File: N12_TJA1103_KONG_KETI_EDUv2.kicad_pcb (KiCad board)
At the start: 2 copper layers, 33 x 57 mm, 65 parts, among them IC1 TJA1103AHN, J1 Conn_02x02_Odd_Even, J2 Conn_02x11_Odd_Even, J3 9-2304372-9, J4 E6S20A-40MT5-Z, Q1 FDN340P, Q2 BSS138, SW2 SW-DIP-ANGLED DS03-254-02BE, Y1 Crystal_GND24_Small

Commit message: fix: finalize native routing and TJA1103 power pin mapping
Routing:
- net Earth: track 24.8 -> 51.6 mm, vias 0 -> 1
- net /TX_EN: track 5.42 -> 26.6 mm, vias 0 -> 2
- net /DP+: track 11.5 -> 20.4 mm, vias 0 -> 1
- net /GP0/CONF0/nLINKLED: track 53.9 -> 56.4 mm
- net /DN-: track 13.7 -> 15.8 mm

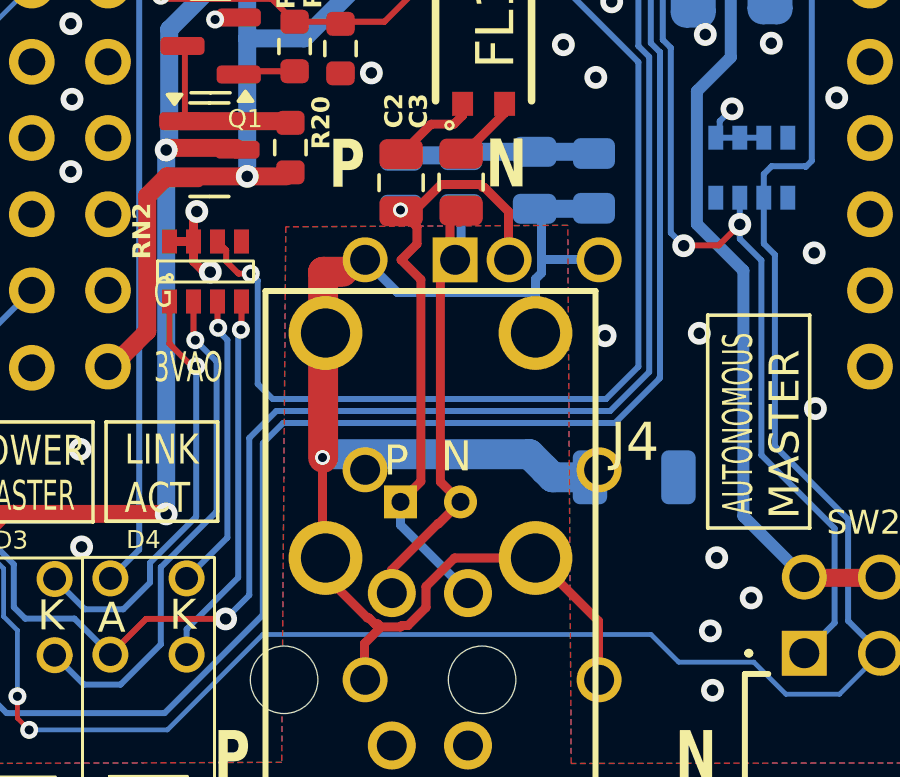
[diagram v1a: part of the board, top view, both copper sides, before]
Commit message: fix: correct MATEnet differential pair polarity
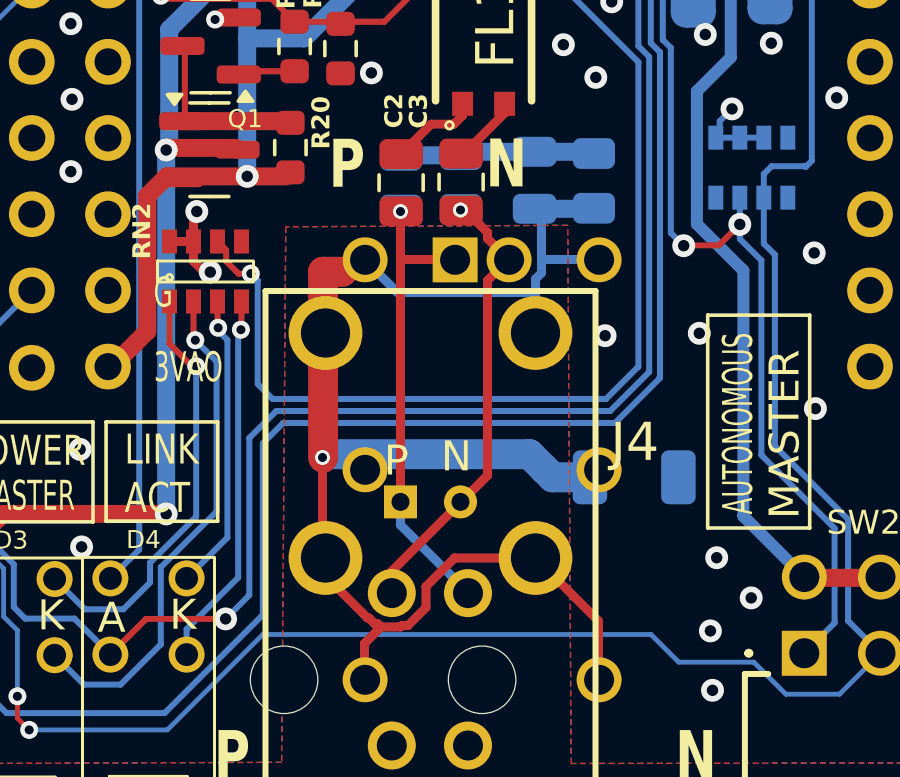
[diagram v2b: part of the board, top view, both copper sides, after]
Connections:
- J3 pad 1: /DN- -> /DP+
- J3 pad 2: /DP+ -> /DN-
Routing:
- net /DP+: track 20.4 -> 15.4 mm
- net /DN-: track 15.8 -> 15.1 mm, vias 0 -> 1
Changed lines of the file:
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@@
 			(layers "*.Cu" "*.Mask")
 			(remove_unused_layers no)
-			(net "/DN-")
+			(net "/DP+")
 			(pinfunction "DN-")
 			(pintype "passive")
@@
 			(layers "*.Cu" "*.Mask")
 			(remove_unused_layers no)
-			(net "/DP+")
+			(net "/DN-")
 			(pinfunction "DP+")
 			(pintype "passive")
@@
 	)
 	(segment
-		(start 16.65 38.79)
-		(end 17.02 39.16)
-		(width 0.3)
-		(layer "F.Cu")
-		(net "/DN-")
-	)
-	(segment
-		(start 16.25 48.15)
-		(end 14.7 49.7)
+		(start 17.15 37.7)
+		(end 17 37.7)
 		(width 0.3)
 		(layer "F.Cu")
@@
 	)
 	(segment
-		(start 16.82 39.36)
-		(end 16.33 39.85)
+		(start 17.9 40.05)
+		(end 17.9 46.55)
 		(width 0.3)
 		(layer "F.Cu")
@@
 	)
 	(segment
-		(start 16.27 48.16)
-		(end 16.25 48.15)
+		(start 17.9 38.65)
+		(end 17.9 38.45)
 		(width 0.3)
 		(layer "F.Cu")
@@
 	)
 	(segment
-		(start 16.65 38.09)
-		(end 16.65 38.79)
+		(start 17 47.45)
+		(end 14.7 49.75)
 		(width 0.3)
 		(layer "F.Cu")
@@
 	)
 	(segment
-		(start 16.33 46.76)
-		(end 17 47.43)
+		(start 17.9 46.55)
+		(end 17 47.45)
 		(width 0.3)
 		(layer "F.Cu")
@@
 	)
 	(segment
-		(start 14.7 49.7)
-		(end 14.7 50.45)
+		(start 17.9 38.45)
+		(end 17.15 37.7)
 		(width 0.3)
 		(layer "F.Cu")
@@
 	)
 	(segment
-		(start 17.02 37.72)
-		(end 16.65 38.09)
+		(start 18.6 39.35)
+		(end 17.9 40.05)
 		(width 0.3)
 		(layer "F.Cu")
@@
 	)
 	(segment
-		(start 16.33 39.85)
-		(end 16.33 46.76)
+		(start 14.7 49.75)
+		(end 14.7 50.45)
 		(width 0.3)
 		(layer "F.Cu")
@@
 	)
 	(segment
-		(start 17 47.43)
-		(end 16.27 48.16)
+		(start 18.6 39.35)
+		(end 17.9 38.65)
 		(width 0.3)
 		(layer "F.Cu")
 		(net "/DN-")
 	)
-	(segment
-		(start 17.02 37.6825)
-		(end 17.02 39.16)
-		(width 0.3)
-		(layer "B.Cu")
+	(via
+		(at 17 37.7)
+		(size 0.5)
+		(drill 0.3)
+		(layers "F.Cu" "B.Cu")
+		(tenting
+			(front yes)
+			(back yes)
+		)
 		(net "/DN-")
 	)
@@
 	)
 	(segment
-		(start 15.25 37.95)
-		(end 16.35 36.85)
-		(width 0.3)
-		(layer "F.Cu")
-		(net "/DP+")
-	)
-	(segment
-		(start 15.02 37.74)
-		(end 15.55 38.27)
-		(width 0.3)
-		(layer "F.Cu")
-		(net "/DP+")
-	)
-	(segment
-		(start 15.55 38.27)
-		(end 15.55 38.83)
-		(width 0.3)
-		(layer "F.Cu")
-		(net "/DP+")
-	)
-	(segment
-		(start 17.8 36.95)
-		(end 18.6 37.75)
-		(width 0.3)
-		(layer "F.Cu")
-		(net "/DP+")
-	)
-	(segment
-		(start 15.68 46.75)
-		(end 15.68 40.02)
-		(width 0.3)
-		(layer "F.Cu")
-		(net "/DP+")
-	)
-	(segment
-		(start 15.55 38.83)
-		(end 15.02 39.36)
-		(width 0.3)
-		(layer "F.Cu")
-		(net "/DP+")
-	)
-	(segment
-		(start 18.6 37.75)
-		(end 18.6 39.35)
-		(width 0.3)
-		(layer "F.Cu")
-		(net "/DP+")
-	)
-	(segment
-		(start 17.75 36.95)
-		(end 17.8 36.95)
-		(width 0.3)
-		(layer "F.Cu")
-		(net "/DP+")
-	)
-	(segment
-		(start 17.65 36.85)
-		(end 17.75 36.95)
-		(width 0.3)
-		(layer "F.Cu")
-		(net "/DP+")
-	)
-	(segment
-		(start 15.68 40.02)
-		(end 15.02 39.36)
-		(width 0.3)
-		(layer "F.Cu")
-		(net "/DP+")
-	)
-	(segment
-		(start 16.35 36.85)
-		(end 17.65 36.85)
+		(start 15 47.45)
+		(end 15 37.75)
 		(width 0.3)
 		(layer "F.Cu")
@@
 	)
 	(segment
-		(start 15 47.43)
-		(end 15.68 46.75)
+		(start 15 39.35)
+		(end 16.8 39.35)
 		(width 0.3)
 		(layer "F.Cu")
@@
 	)
 	(via
-		(at 15 37.7)
+		(at 15 37.75)
 		(size 0.5)
 		(drill 0.3)
